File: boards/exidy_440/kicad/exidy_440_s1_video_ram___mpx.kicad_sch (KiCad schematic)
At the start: 11 parts

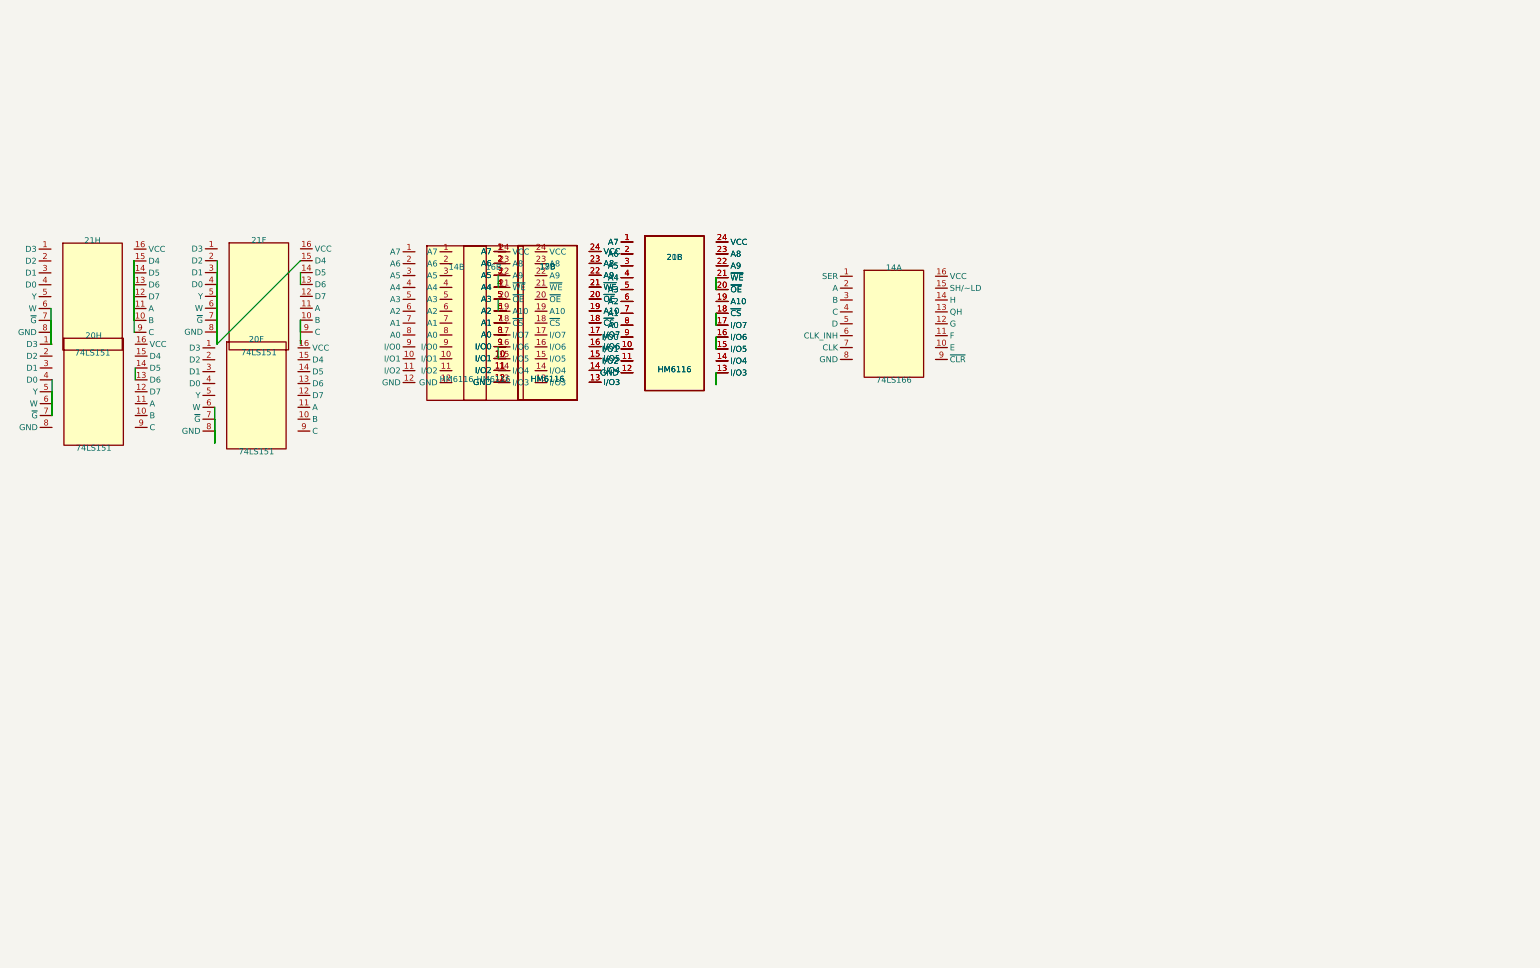
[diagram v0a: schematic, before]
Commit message: kicad export: emit Footprint property mapped from librarian package
Adds PACKAGE_TO_KICAD_FP table mapping librarian `package` strings
("DIP-14", "DIP-40", …) to KiCad stock footprint ids ("Package_DIP:
DIP-14_W7.62mm", "Package_DIP:DIP-40_W15.24mm", …). The table covers
every package currently in chips.json. Width convention: ≤20 pins →
0.3" (W7.62mm), ≥24 pins → 0.6" (W15.24mm), which matches the actual
chips in our librarian (≥24-pin parts are all memory/CPU, always 0.6"-
wide DIPs). Parts can override with an explicit `kicad_footprint`
field if a future chip breaks the rule.

Both lib_symbols and instance properties carry the footprint, so
`kicad-cli sch export bom` reports the correct land pattern per refdes.
No PCB-side library config needed — Package_DIP ships with KiCad.

Verified on dorado_base sheet 5 (still ERC PASS) and exidy_440 sheet 1
(blocking=0 unchanged); BOMs show every component mapped correctly.

Co-Authored-By: Claude Opus 4.7 (1M context) <noreply@anthropic.com>
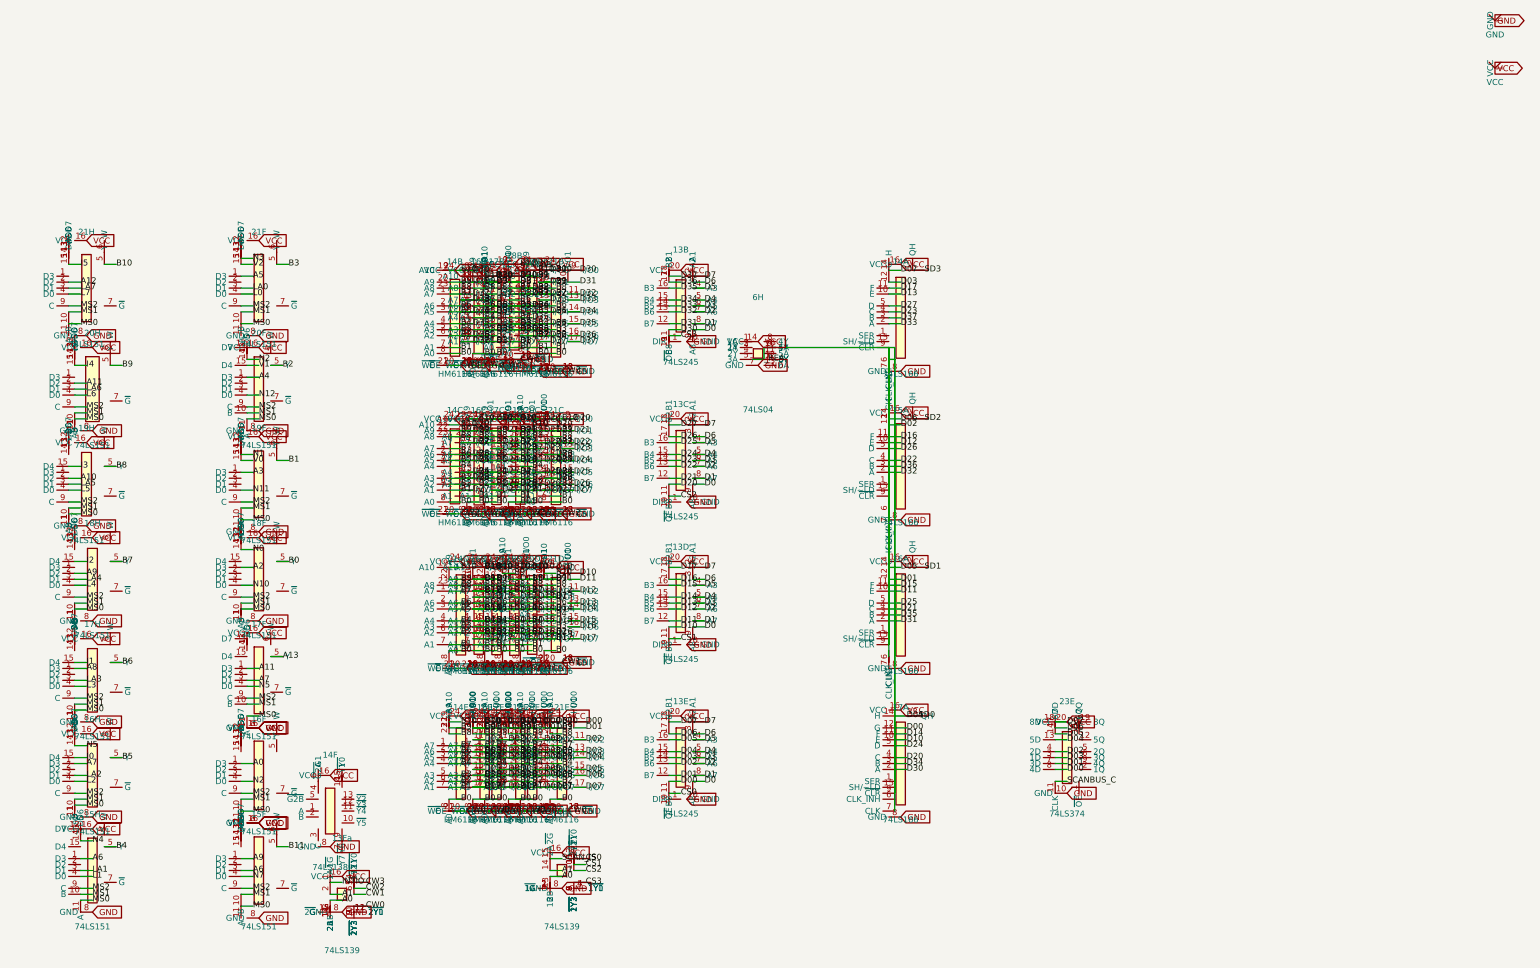
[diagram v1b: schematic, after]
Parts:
- added 13B: 74LS245, Package_DIP:DIP-20_W7.62mm, symbol user:_chip_13B
- added 13C: 74LS245, Package_DIP:DIP-20_W7.62mm, symbol user:_chip_13C
- added 13D: 74LS245, Package_DIP:DIP-20_W7.62mm, symbol user:_chip_13D
- added 13E: 74LS245, Package_DIP:DIP-20_W7.62mm, symbol user:_chip_13E
- added 13Fa: 74LS139, Package_DIP:DIP-16_W7.62mm, symbol user:_chip_13Fa
- added 13Fb: 74LS139, Package_DIP:DIP-16_W7.62mm, symbol user:_chip_13Fb
- added 14C: HM6116, Package_DIP:DIP-24_W15.24mm, symbol user:_chip_14C
- added 14D: HM6116, Package_DIP:DIP-24_W15.24mm, symbol user:_chip_14D
- added 14E: HM6116, Package_DIP:DIP-24_W15.24mm, symbol user:_chip_14E
- added 14F: 74LS138, Package_DIP:DIP-16_W7.62mm, symbol user:_chip_14F
- added 15A: 74LS166, Package_DIP:DIP-16_W7.62mm, symbol user:_chip_15A
- added 15F: 74LS151, Package_DIP:DIP-16_W7.62mm, symbol user:_chip_15F
- added 15H: 74LS151, Package_DIP:DIP-16_W7.62mm, symbol user:_chip_15H
- added 16A: 74LS166, Package_DIP:DIP-16_W7.62mm, symbol user:_chip_16A
- added 16C: HM6116, Package_DIP:DIP-24_W15.24mm, symbol user:_chip_16C
- added 16D: HM6116, Package_DIP:DIP-24_W15.24mm, symbol user:_chip_16D
- added 16E: HM6116, Package_DIP:DIP-24_W15.24mm, symbol user:_chip_16E
- added 16F: 74LS151, Package_DIP:DIP-16_W7.62mm, symbol user:_chip_16F
- added 16H: 74LS151, Package_DIP:DIP-16_W7.62mm, symbol user:_chip_16H
- added 17A: 74LS166, Package_DIP:DIP-16_W7.62mm, symbol user:_chip_17A
- added 17C: HM6116, Package_DIP:DIP-24_W15.24mm, symbol user:_chip_17C
- added 17D: HM6116, Package_DIP:DIP-24_W15.24mm, symbol user:_chip_17D
- added 17E: HM6116, Package_DIP:DIP-24_W15.24mm, symbol user:_chip_17E
- added 17F: 74LS151, Package_DIP:DIP-16_W7.62mm, symbol user:_chip_17F
- added 17H: 74LS151, Package_DIP:DIP-16_W7.62mm, symbol user:_chip_17H
- added 18C: HM6116, Package_DIP:DIP-24_W15.24mm, symbol user:_chip_18C
- added 18D: HM6116, Package_DIP:DIP-24_W15.24mm, symbol user:_chip_18D
- added 18E: HM6116, Package_DIP:DIP-24_W15.24mm, symbol user:_chip_18E
- added 18F: 74LS151, Package_DIP:DIP-16_W7.62mm, symbol user:_chip_18F
- added 18H: 74LS151, Package_DIP:DIP-16_W7.62mm, symbol user:_chip_18H
- added 19F: 74LS151, Package_DIP:DIP-16_W7.62mm, symbol user:_chip_19F
- added 19H: 74LS151, Package_DIP:DIP-16_W7.62mm, symbol user:_chip_19H
- added 20C: HM6116, Package_DIP:DIP-24_W15.24mm, symbol user:_chip_20C
- added 20D: HM6116, Package_DIP:DIP-24_W15.24mm, symbol user:_chip_20D
- added 20E: HM6116, Package_DIP:DIP-24_W15.24mm, symbol user:_chip_20E
- added 21C: HM6116, Package_DIP:DIP-24_W15.24mm, symbol user:_chip_21C
- added 21D: HM6116, Package_DIP:DIP-24_W15.24mm, symbol user:_chip_21D
- added 21E: HM6116, Package_DIP:DIP-24_W15.24mm, symbol user:_chip_21E
- added 23E: 74LS374, Package_DIP:DIP-20_W7.62mm, symbol user:_chip_23E
- added 6H: 74LS04, Package_DIP:DIP-14_W7.62mm, symbol user:_chip_6H
- 14A: footprint (none) -> Package_DIP:DIP-16_W7.62mm; symbol user:74LS166 -> user:_chip_14A
- 14B: footprint (none) -> Package_DIP:DIP-24_W15.24mm; symbol user:HM6116 -> user:_chip_14B
- 16B: footprint (none) -> Package_DIP:DIP-24_W15.24mm; symbol user:HM6116 -> user:_chip_16B
- 17B: footprint (none) -> Package_DIP:DIP-24_W15.24mm; symbol user:HM6116 -> user:_chip_17B
- 18B: footprint (none) -> Package_DIP:DIP-24_W15.24mm; symbol user:HM6116 -> user:_chip_18B
- 20B: footprint (none) -> Package_DIP:DIP-24_W15.24mm; symbol user:HM6116 -> user:_chip_20B
- 20F: footprint (none) -> Package_DIP:DIP-16_W7.62mm; symbol user:74LS151 -> user:_chip_20F
- 20H: footprint (none) -> Package_DIP:DIP-16_W7.62mm; symbol user:74LS151 -> user:_chip_20H
- 21B: footprint (none) -> Package_DIP:DIP-24_W15.24mm; symbol user:HM6116 -> user:_chip_21B
- 21F: footprint (none) -> Package_DIP:DIP-16_W7.62mm; symbol user:74LS151 -> user:_chip_21F
- 21H: footprint (none) -> Package_DIP:DIP-16_W7.62mm; symbol user:74LS151 -> user:_chip_21H
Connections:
- net GND: now reaches 17B.1 (A7), 18B.1 (A7)
- net GND: now also 14A.10 (E), 14A.11 (F), 14A.12 (G), 14A.14 (H), 14A.16 (VCC), 14A.2 (A), 14A.3 (B), 14A.4 (C), 14A.5 (D), 14A.8 (GND), 14B.1 (A7), 14B.10 (I/O1), 14B.11 (I/O2), 14B.12 (GND), 14B.13 (I/O3), 14B.14 (I/O4), 14B.15 (I/O5), 14B.16 (I/O6), 14B.17 (I/O7), 14B.18 (~{CS}), 14B.19 (A10), 14B.2 (A6), 14B.21 (~{WE}), 14B.22 (A9), 14B.23 (A8), 14B.24 (VCC), 14B.3 (A5), 14B.4 (A4), 14B.5 (A3), 14B.6 (A2), 14B.7 (A1), 14B.9 (I/O0), 16B.1 (A7), 16B.10 (I/O1), 16B.11 (I/O2), 16B.12 (GND), 16B.13 (I/O3), 16B.14 (I/O4), 16B.15 (I/O5), 16B.16 (I/O6), 16B.17 (I/O7), 16B.18 (~{CS}), 16B.19 (A10), 16B.2 (A6), 16B.21 (~{WE}), 16B.22 (A9), 16B.23 (A8), 16B.24 (VCC), 16B.3 (A5), 16B.4 (A4), 16B.5 (A3), 16B.6 (A2), 16B.7 (A1), 16B.9 (I/O0), 17B.10 (I/O1), 17B.11 (I/O2), 17B.12 (GND), 17B.13 (I/O3), 17B.14 (I/O4), 17B.15 (I/O5), 17B.16 (I/O6), 17B.17 (I/O7), 17B.18 (~{CS}), 17B.19 (A10), 17B.2 (A6), 17B.21 (~{WE}), 17B.22 (A9), 17B.23 (A8), 17B.24 (VCC), 17B.3 (A5), 17B.4 (A4), 17B.5 (A3), 17B.6 (A2), 17B.7 (A1), 17B.9 (I/O0), 18B.10 (I/O1), 18B.11 (I/O2), 18B.12 (GND), 18B.13 (I/O3), 18B.14 (I/O4), 18B.15 (I/O5), 18B.16 (I/O6), 18B.17 (I/O7), 18B.18 (~{CS}), 18B.19 (A10), 18B.2 (A6), 18B.21 (~{WE}), 18B.22 (A9), 18B.23 (A8), 18B.24 (VCC), 18B.3 (A5), 18B.4 (A4), 18B.5 (A3), 18B.6 (A2), 18B.7 (A1), 18B.9 (I/O0), 20B.1 (A7), 20B.10 (I/O1), 20B.11 (I/O2), 20B.12 (GND), 20B.13 (I/O3), 20B.14 (I/O4), 20B.15 (I/O5), 20B.16 (I/O6), 20B.17 (I/O7), 20B.18 (~{CS}), 20B.19 (A10), 20B.2 (A6), 20B.21 (~{WE}), 20B.22 (A9), 20B.23 (A8), 20B.24 (VCC), 20B.3 (A5), 20B.4 (A4), 20B.5 (A3), 20B.6 (A2), 20B.7 (A1), 20B.9 (I/O0), 20F.16 (VCC), 20F.5 (Y), 20F.8 (GND), 20H.16 (VCC), 20H.5 (Y), 20H.8 (GND), 21B.1 (A7), 21B.10 (I/O1), 21B.11 (I/O2), 21B.12 (GND), 21B.13 (I/O3), 21B.14 (I/O4), 21B.15 (I/O5), 21B.16 (I/O6), 21B.17 (I/O7), 21B.18 (~{CS}), 21B.19 (A10), 21B.2 (A6), 21B.21 (~{WE}), 21B.22 (A9), 21B.23 (A8), 21B.24 (VCC), 21B.3 (A5), 21B.4 (A4), 21B.5 (A3), 21B.6 (A2), 21B.7 (A1), 21B.9 (I/O0), 21F.16 (VCC), 21F.5 (Y), 21F.8 (GND), 21H.16 (VCC), 21H.5 (Y), 21H.8 (GND), 13B.10 (GND), 13B.11 (B8), 13B.12 (B7), 13B.13 (B6), 13B.14 (B5), 13B.15 (B4), 13B.16 (B3), 13B.17 (B2), 13B.18 (B1), 13B.20 (VCC), 13C.10 (GND), 13C.11 (B8), 13C.12 (B7), 13C.13 (B6), 13C.14 (B5), 13C.15 (B4), 13C.16 (B3), 13C.17 (B2), 13C.18 (B1), 13C.20 (VCC), 13D.10 (GND), 13D.11 (B8), 13D.12 (B7), 13D.13 (B6), 13D.14 (B5), 13D.15 (B4), 13D.16 (B3), 13D.17 (B2), 13D.18 (B1), 13D.20 (VCC), 13E.10 (GND), 13E.11 (B8), 13E.12 (B7), 13E.14 (B5), 13E.15 (B4), 13E.17 (B2), 13E.18 (B1), 13E.20 (VCC), 13Fa.10 (~{2Y2}), 13Fa.16 (VCC), 13Fa.4 (~{1Y0}), 13Fa.5 (~{1Y1}), 13Fa.6 (~{1Y2}), 13Fa.7 (~{1Y3}), 13Fa.8 (GND), 13Fa.9 (~{2Y3}), 13Fb.16 (VCC), 13Fb.8 (GND), 14C.1 (A7), 14C.10 (I/O1), 14C.11 (I/O2), 14C.12 (GND), 14C.13 (I/O3), 14C.14 (I/O4), 14C.15 (I/O5), 14C.16 (I/O6), 14C.17 (I/O7), 14C.18 (~{CS}), 14C.19 (A10), 14C.2 (A6), 14C.21 (~{WE}), 14C.22 (A9), 14C.23 (A8), 14C.24 (VCC), 14C.3 (A5), 14C.4 (A4), 14C.5 (A3), 14C.6 (A2), 14C.7 (A1), 14C.9 (I/O0), 14D.1 (A7), 14D.10 (I/O1), 14D.11 (I/O2), 14D.12 (GND), 14D.13 (I/O3), 14D.14 (I/O4), 14D.15 (I/O5), 14D.16 (I/O6), 14D.17 (I/O7), 14D.18 (~{CS}), 14D.19 (A10), 14D.2 (A6), 14D.21 (~{WE}), 14D.22 (A9), 14D.23 (A8), 14D.24 (VCC), 14D.3 (A5), 14D.4 (A4), 14D.5 (A3), 14D.6 (A2), 14D.7 (A1), 14D.9 (I/O0), 14E.1 (A7), 14E.10 (I/O1), 14E.12 (GND), 14E.13 (I/O3), 14E.14 (I/O4), 14E.16 (I/O6), 14E.17 (I/O7), 14E.18 (~{CS}), 14E.19 (A10), 14E.2 (A6), 14E.21 (~{WE}), 14E.22 (A9), 14E.23 (A8), 14E.24 (VCC), 14E.3 (A5), 14E.4 (A4), 14E.5 (A3), 14E.6 (A2), 14E.7 (A1), 14E.9 (I/O0), 14F.16 (VCC), 14F.8 (GND), 15A.10 (E), 15A.11 (F), 15A.14 (H), 15A.16 (VCC), 15A.2 (A), 15A.3 (B), 15A.4 (C), 15A.5 (D), 15A.8 (GND), 15F.16 (VCC), 15F.8 (GND), 15H.16 (VCC), 15H.5 (Y), 15H.8 (GND), 16A.10 (E), 16A.11 (F), 16A.12 (G), 16A.16 (VCC), 16A.2 (A), 16A.3 (B), 16A.4 (C), 16A.5 (D), 16A.8 (GND), 16C.1 (A7), 16C.10 (I/O1), 16C.11 (I/O2), 16C.12 (GND), 16C.13 (I/O3), 16C.14 (I/O4), 16C.15 (I/O5), 16C.16 (I/O6), 16C.17 (I/O7), 16C.18 (~{CS}), 16C.19 (A10), 16C.2 (A6), 16C.21 (~{WE}), 16C.22 (A9), 16C.23 (A8), 16C.24 (VCC), 16C.3 (A5), 16C.4 (A4), 16C.5 (A3), 16C.6 (A2), 16C.7 (A1), 16C.9 (I/O0), 16D.1 (A7), 16D.10 (I/O1), 16D.11 (I/O2), 16D.12 (GND), 16D.13 (I/O3), 16D.14 (I/O4), 16D.15 (I/O5), 16D.16 (I/O6), 16D.17 (I/O7), 16D.18 (~{CS}), 16D.19 (A10), 16D.2 (A6), 16D.21 (~{WE}), 16D.22 (A9), 16D.23 (A8), 16D.24 (VCC), 16D.3 (A5), 16D.4 (A4), 16D.5 (A3), 16D.6 (A2), 16D.7 (A1), 16D.9 (I/O0), 16E.1 (A7), 16E.10 (I/O1), 16E.12 (GND), 16E.13 (I/O3), 16E.14 (I/O4), 16E.16 (I/O6), 16E.17 (I/O7), 16E.18 (~{CS}), 16E.19 (A10), 16E.2 (A6), 16E.21 (~{WE}), 16E.22 (A9), 16E.23 (A8), 16E.24 (VCC), 16E.3 (A5), 16E.4 (A4), 16E.5 (A3), 16E.6 (A2), 16E.7 (A1), 16E.9 (I/O0), 16F.16 (VCC), 16F.8 (GND), 16H.16 (VCC), 16H.5 (Y), 16H.8 (GND), 17A.10 (E), 17A.11 (F), 17A.12 (G), 17A.13 (QH), 17A.14 (H), 17A.16 (VCC), 17A.2 (A), 17A.3 (B), 17A.4 (C), 17A.5 (D), 17A.8 (GND), 17C.1 (A7), 17C.10 (I/O1), 17C.11 (I/O2), 17C.12 (GND), 17C.13 (I/O3), 17C.14 (I/O4), 17C.15 (I/O5), 17C.16 (I/O6), 17C.17 (I/O7), 17C.18 (~{CS}), 17C.19 (A10), 17C.2 (A6), 17C.21 (~{WE}), 17C.22 (A9), 17C.23 (A8), 17C.24 (VCC), 17C.3 (A5), 17C.4 (A4), 17C.5 (A3), 17C.6 (A2), 17C.7 (A1), 17C.9 (I/O0), 17D.1 (A7), 17D.10 (I/O1), 17D.11 (I/O2), 17D.12 (GND), 17D.13 (I/O3), 17D.14 (I/O4), 17D.15 (I/O5), 17D.16 (I/O6), 17D.17 (I/O7)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
- net at 17B.20 (~{OE}): no longer 18B.20 (~{OE})
- net B0: now reaches 17B.8 (A0), 18B.8 (A0)
- net B0: now also 14B.8 (A0), 16B.8 (A0), 20B.8 (A0), 21B.8 (A0), 14C.8 (A0), 14D.8 (A0), 14E.8 (A0), 16C.8 (A0), 16D.8 (A0), 16E.8 (A0), 17C.8 (A0), 17D.8 (A0), 17E.8 (A0), 18C.8 (A0), 18D.8 (A0), 18E.8 (A0), 18F.5 (Y), 20C.8 (A0), 20D.8 (A0), 20E.8 (A0), 21C.8 (A0), 21D.8 (A0), 21E.8 (A0)
- net A12: now reaches 21H.2 (D2)
- net LA7: now reaches 21H.3 (D1)
- net L7: now reaches 21H.4 (D0)
- net at 14B.20 (~{OE}): no longer 14B.19 (A10)
- net A5: now reaches 21F.1 (D3)
- net MS1: now reaches 21F.10 (B)
- net MS1: now also 20F.10 (B), 20H.10 (B), 21H.10 (B), 15F.10 (B), 15H.10 (B), 16F.10 (B), 16H.10 (B), 17F.10 (B), 17H.10 (B), 18F.10 (B), 18H.10 (B), 19F.10 (B), 19H.10 (B); no longer 21F.9 (C)
- net MS0: now reaches 21F.11 (A)
- net MS0: now also 20F.11 (A), 20H.11 (A), 21H.11 (A), 15F.11 (A), 15H.11 (A), 16F.11 (A), 16H.11 (A), 17F.11 (A), 17H.11 (A), 18F.11 (A), 18H.11 (A), 19F.11 (A), 19H.11 (A)
- net at 21F.13 (D6): no longer 21F.14 (D5)
- net A4: now reaches 20F.1 (D3)
- net N2: now reaches 20F.14 (D5)
- net N2: now also 16F.4 (D0)
- net V1: now reaches 20F.15 (D4)
- net N12: now reaches 20F.4 (D0)
- net MS2: now reaches 20F.9 (C)
- net MS2: now also 20H.9 (C), 21F.9 (C), 21H.9 (C), 15F.9 (C), 15H.9 (C), 16F.9 (C), 16H.9 (C), 17F.9 (C), 17H.9 (C), 18F.9 (C), 18H.9 (C), 19F.9 (C), 19H.9 (C)
- net SD3: now reaches 14A.13 (QH)
- net _REA: now reaches 14A.7 (CLK)
- net _REA: now also 14A.9 (~{CLR}), 15A.7 (CLK), 15A.9 (~{CLR}), 16A.7 (CLK), 16A.9 (~{CLR}), 17A.7 (CLK), 17A.9 (~{CLR}), 6H.10 (5Y), 6H.12 (6Y), 6H.5 (3A), 6H.6 (3Y), 6H.9 (4A)
- net at 20H.13 (D6): no longer 20H.14 (D5)
- net I4: now reaches 20H.15 (D4)
- net A11: now reaches 20H.2 (D2)
- net A11: now also 17F.1 (D3)
- net LA6: now reaches 20H.3 (D1)
- net L6: now reaches 20H.4 (D0)
- new net: 6H.2 (1Y), 6H.3 (2A)
- new net: 13Fa.11 (~{2Y1}), 13Fa.12 (~{2Y0})
- new net: 13Fa.13 (2B), 13Fa.14 (2A)
- new net: 13Fb.1 (~{1G}), 13Fb.2 (1A)
- new net: 13Fb.4 (~{1Y0}), 13Fb.5 (~{1Y1})
- new net A0: 13Fa.3 (1B), 13Fb.13 (2B), 16F.1 (D3)
- new net A1: 13Fa.2 (1A), 13Fb.14 (2A)
- new net A10: 19H.2 (D2)
- new net A13: 17F.5 (Y)
- new net A2: 18F.1 (D3)
- new net A3: 19F.1 (D3)
- new net A6: 15F.3 (D1), 15H.1 (D3)
- new net A7: 16H.1 (D3), 17F.3 (D1)
- new net A8: 17H.1 (D3)
- new net A9: 15F.1 (D3), 18H.2 (D2)
- new net B11: 15F.5 (Y)
- new net CS0: 13E.19 (~{OE}), 13Fb.12 (~{2Y0})
- new net CS1: 13D.19 (~{OE}), 13Fb.11 (~{2Y1})
- new net CS2: 13C.19 (~{OE}), 13Fb.10 (~{2Y2})
- new net CS3: 13B.19 (~{OE}), 13Fb.6 (~{1Y2}), 13Fb.7 (~{1Y3}), 13Fb.9 (~{2Y3})
- new net D0: 13B.9 (A8), 13C.9 (A8), 13D.9 (A8), 13E.9 (A8)
- new net D02: 13E.13 (B6), 14E.11 (I/O2), 15A.12 (G), 16E.11 (I/O2), 17E.11 (I/O2), 18E.11 (I/O2), 20E.11 (I/O2), 21E.11 (I/O2), 23E.4 (2D)
- new net D05: 13E.16 (B3), 14E.15 (I/O5), 16A.14 (H), 16E.15 (I/O5), 17E.15 (I/O5), 18E.15 (I/O5), 20E.15 (I/O5), 21E.15 (I/O5), 23E.14 (6D)
- new net D1: 13B.8 (A7), 13C.8 (A7), 13D.8 (A7), 13E.8 (A7)
- new net D2: 13B.7 (A6), 13C.7 (A6), 13D.7 (A6), 13E.7 (A6)
- new net D3: 13B.6 (A5), 13C.6 (A5), 13D.6 (A5), 13E.6 (A5)
- new net D4: 13B.5 (A4), 13C.5 (A4), 13D.5 (A4), 13E.5 (A4)
- new net D5: 13B.4 (A3), 13C.4 (A3), 13D.4 (A3), 13E.4 (A3)
- new net D6: 13B.3 (A2), 13C.3 (A2), 13D.3 (A2), 13E.3 (A2)
- new net D7: 13B.2 (A1), 13C.2 (A1), 13D.2 (A1), 13E.2 (A1)
- new net I0: 16H.15 (D4)
- new net I1: 17H.15 (D4)
- new net I2: 18H.15 (D4)
- new net I3: 19H.15 (D4)
- new net I5: 21H.15 (D4)
- new net INTIO: 13Fa.1 (~{1G})
- new net L0: 21F.4 (D0)
- new net L1: 15H.4 (D0)
- new net L2: 16H.4 (D0)
- new net L3: 17H.4 (D0)
- new net L4: 18H.4 (D0)
- new net L5: 19H.4 (D0)
- new net LA0: 21F.3 (D1)
- new net LA1: 15H.3 (D1)
- new net LA2: 16H.3 (D1)
- new net LA3: 17H.3 (D1)
- new net LA4: 18H.3 (D1)
- new net LA5: 19H.3 (D1)
- new net N0: 18F.14 (D5)
- new net N1: 19F.14 (D5)
- new net N10: 18F.4 (D0)
- new net N11: 19F.4 (D0)
- new net N3: 21F.14 (D5)
- new net N4: 15H.14 (D5)
- new net N5: 16H.14 (D5), 17F.4 (D0)
- new net N7: 15F.4 (D0)
- new net SCANBUS_C: 23E.11 (CLK)
- new net SCAN_IS: 13Fb.15 (~{2G})
- new net SD1: 16A.13 (QH)
- new net SD2: 15A.13 (QH)
- new net V0: 19F.15 (D4)
- new net V2: 21F.15 (D4)
- now unconnected: 20B.20 (~{OE}), 20F.6 (W), 20F.7 (~{G}), 21B.20 (~{OE}), 21F.2 (D2), 21F.6 (W), 21F.7 (~{G}), 21H.12 (D7), 21H.13 (D6), 21H.14 (D5)
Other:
- moved on the sheet: 14A, 20F, 20H, 21F, 21H

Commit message: kicad export: fix pin-tip / polyline snap mismatch (1.27 mm off-grid)
Two code paths emitted absolute mm coords differently:

  pin tip   = _snap(M + cx_px*s) + _snap((ix-cx_px)*s)      # double-snap
  polyline  = _snap(M + p[0]*s)                              # single-snap

`_snap(a) + _snap(b) != _snap(a+b)` in general — the difference is 0 or
±1 grid unit. On Z80 SBC, a hand-traced wire from J1.2 to U1.14 had its
endpoint at the polyline's snapped coord (71.12, 76.20) while the pin
tip lived at the double-snapped coord (72.39, 74.93). KiCad reported
wire_dangling and 8 other short wires had the same workaround applied
(converted to label nets to dodge it).

Fix:
- synth_faithful_symbol now derives lib-symbol pin coords from the
  absolute pin tip (single-snap) minus the instance origin, instead of
  snapping the local offset directly. The local pin offset is no longer
  guaranteed to be a whole grid unit — body and pin can drift up to
  ~0.6 mm relative to each other — but the absolute pin tip is now
  always on grid AND agrees with every other coord-emitting path.
- gen_sch's faithful branch uses the same single-snap formula for
  pin_endpoint_mm.

This makes pin tips, polyline points, junctions, and discrete pins all
share one snap convention. Validated on Z80 SBC: RS232_TX (a workaround
label) converted back to wire + path produces wire_dangling=0.

Regression: dorado_base sheets 5/7/8, z80_sbc sheet 1, exidy_440 sheet 1
all stay blocking=0. Pre-existing graph wiring errors (pin_to_pin,
multiple_net_names) unchanged.

Removes bugs/polyline-pin-snap-mismatch.md.

Co-Authored-By: Claude Opus 4.7 (1M context) <noreply@anthropic.com>
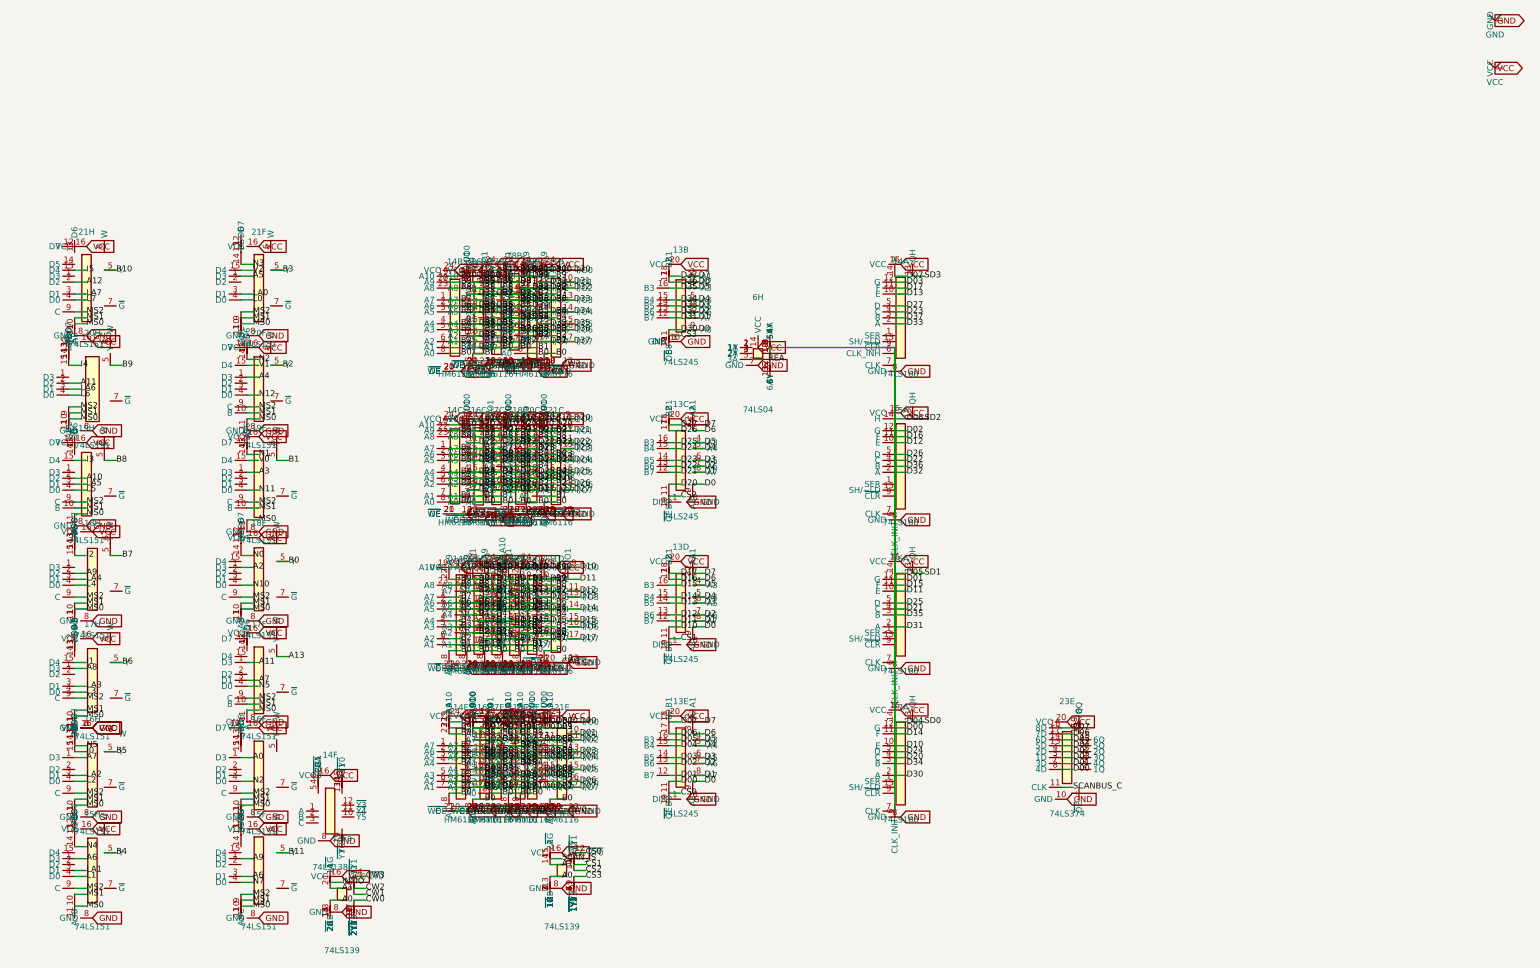
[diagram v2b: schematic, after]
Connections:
- net CS3: no longer 13Fb.6 (~{1Y2}), 13Fb.7 (~{1Y3})
- net GND: now also 13B.1 (DIR), 14B.20 (~{OE}), 14C.20 (~{OE}), 16B.20 (~{OE}), 17E.20 (~{OE}), 20B.20 (~{OE}); no longer 13B.12 (B7), 13B.13 (B6), 13B.14 (B5), 13B.15 (B4), 13B.16 (B3), 13B.17 (B2), 13B.18 (B1), 13C.12 (B7), 13C.13 (B6), 13C.14 (B5), 13C.15 (B4), 13C.16 (B3), 13C.17 (B2), 13C.18 (B1), 13D.12 (B7), 13D.13 (B6), 13D.14 (B5), 13D.15 (B4), 13D.16 (B3), 13D.17 (B2), 13D.18 (B1), 13E.12 (B7), 13E.14 (B5), 13E.15 (B4), 13E.17 (B2), 13E.18 (B1), 13Fa.10 (~{2Y2}), 13Fa.9 (~{2Y3}), 14A.10 (E), 14A.11 (F), 14A.12 (G), 14A.14 (H), 14A.2 (A), 14A.3 (B), 14A.4 (C), 14A.5 (D), 14B.1 (A7), 14B.10 (I/O1), 14B.11 (I/O2), 14B.13 (I/O3), 14B.14 (I/O4), 14B.15 (I/O5), 14B.16 (I/O6), 14B.17 (I/O7), 14B.2 (A6), 14B.22 (A9), 14B.23 (A8), 14B.3 (A5), 14B.4 (A4), 14B.5 (A3), 14B.6 (A2), 14B.7 (A1), 14C.1 (A7), 14C.10 (I/O1), 14C.11 (I/O2), 14C.13 (I/O3), 14C.14 (I/O4), 14C.15 (I/O5), 14C.16 (I/O6), 14C.17 (I/O7), 14C.18 (~{CS}), 14C.2 (A6), 14C.22 (A9), 14C.23 (A8), 14C.3 (A5), 14C.4 (A4), 14C.5 (A3), 14C.6 (A2), 14C.7 (A1), 14D.1 (A7), 14D.10 (I/O1), 14D.11 (I/O2), 14D.13 (I/O3), 14D.14 (I/O4), 14D.15 (I/O5), 14D.16 (I/O6), 14D.17 (I/O7), 14D.2 (A6), 14D.22 (A9), 14D.23 (A8), 14D.3 (A5), 14D.4 (A4), 14D.5 (A3), 14D.6 (A2), 14D.7 (A1), 14E.1 (A7), 14E.10 (I/O1), 14E.13 (I/O3), 14E.14 (I/O4), 14E.16 (I/O6), 14E.17 (I/O7), 14E.2 (A6), 14E.22 (A9), 14E.23 (A8), 14E.3 (A5), 14E.4 (A4), 14E.5 (A3), 14E.6 (A2), 14E.7 (A1), 15A.10 (E), 15A.11 (F), 15A.14 (H), 15A.2 (A), 15A.3 (B), 15A.4 (C), 15A.5 (D), 15H.5 (Y), 16A.10 (E), 16A.11 (F), 16A.12 (G), 16A.2 (A), 16A.3 (B), 16A.4 (C), 16A.5 (D), 16B.1 (A7), 16B.10 (I/O1), 16B.11 (I/O2), 16B.13 (I/O3), 16B.14 (I/O4), 16B.15 (I/O5), 16B.16 (I/O6), 16B.17 (I/O7), 16B.2 (A6), 16B.22 (A9), 16B.23 (A8), 16B.3 (A5), 16B.4 (A4), 16B.5 (A3), 16B.6 (A2), 16B.7 (A1), 16C.1 (A7), 16C.10 (I/O1), 16C.11 (I/O2), 16C.13 (I/O3), 16C.14 (I/O4), 16C.15 (I/O5), 16C.16 (I/O6), 16C.17 (I/O7), 16C.2 (A6), 16C.22 (A9), 16C.23 (A8), 16C.3 (A5), 16C.4 (A4), 16C.5 (A3), 16C.6 (A2), 16C.7 (A1), 16D.1 (A7), 16D.10 (I/O1), 16D.11 (I/O2), 16D.13 (I/O3), 16D.14 (I/O4), 16D.15 (I/O5), 16D.16 (I/O6), 16D.17 (I/O7), 16D.2 (A6), 16D.22 (A9), 16D.23 (A8), 16D.3 (A5), 16D.4 (A4), 16D.5 (A3), 16D.6 (A2), 16D.7 (A1), 16E.1 (A7), 16E.10 (I/O1), 16E.13 (I/O3), 16E.14 (I/O4), 16E.16 (I/O6), 16E.17 (I/O7), 16E.18 (~{CS}), 16E.2 (A6), 16E.22 (A9), 16E.23 (A8), 16E.3 (A5), 16E.4 (A4), 16E.5 (A3), 16E.6 (A2), 16E.7 (A1), 16H.5 (Y), 17A.11 (F), 17A.13 (QH), 17A.14 (H), 17A.3 (B), 17A.5 (D), 17B.1 (A7), 17B.10 (I/O1), 17B.11 (I/O2), 17B.13 (I/O3), 17B.14 (I/O4), 17B.15 (I/O5), 17B.16 (I/O6), 17B.17 (I/O7), 17B.2 (A6), 17B.22 (A9), 17B.23 (A8), 17B.3 (A5), 17B.4 (A4), 17B.5 (A3), 17B.6 (A2), 17B.7 (A1), 17C.1 (A7), 17C.10 (I/O1), 17C.11 (I/O2), 17C.13 (I/O3), 17C.14 (I/O4), 17C.15 (I/O5), 17C.16 (I/O6), 17C.17 (I/O7), 17C.2 (A6), 17C.22 (A9), 17C.23 (A8), 17C.3 (A5), 17C.4 (A4), 17C.5 (A3), 17C.6 (A2), 17C.7 (A1), 17D.1 (A7), 17D.10 (I/O1), 17D.11 (I/O2), 17D.13 (I/O3), 17D.14 (I/O4), 17D.15 (I/O5), 17D.16 (I/O6), 17D.17 (I/O7), 17D.2 (A6), 17D.22 (A9), 17D.23 (A8), 17D.3 (A5), 17D.4 (A4), 17D.5 (A3), 17D.6 (A2), 17D.7 (A1), 17E.1 (A7), 17E.10 (I/O1), 17E.13 (I/O3), 17E.14 (I/O4), 17E.16 (I/O6), 17E.17 (I/O7), 17E.18 (~{CS}), 17E.2 (A6), 17E.22 (A9), 17E.23 (A8), 17E.3 (A5), 17E.4 (A4), 17E.5 (A3), 17E.6 (A2), 17E.7 (A1), 17H.5 (Y), 18B.1 (A7), 18B.10 (I/O1), 18B.11 (I/O2), 18B.13 (I/O3), 18B.14 (I/O4), 18B.15 (I/O5), 18B.16 (I/O6), 18B.17 (I/O7), 18B.2 (A6), 18B.22 (A9), 18B.23 (A8), 18B.3 (A5), 18B.4 (A4), 18B.5 (A3), 18B.6 (A2), 18B.7 (A1), 18C.1 (A7), 18C.10 (I/O1), 18C.11 (I/O2), 18C.13 (I/O3), 18C.14 (I/O4), 18C.15 (I/O5), 18C.16 (I/O6), 18C.17 (I/O7), 18C.18 (~{CS}), 18C.2 (A6), 18C.22 (A9), 18C.23 (A8), 18C.3 (A5), 18C.4 (A4), 18C.5 (A3), 18C.6 (A2), 18C.7 (A1), 18D.1 (A7), 18D.10 (I/O1), 18D.11 (I/O2), 18D.13 (I/O3), 18D.14 (I/O4), 18D.15 (I/O5), 18D.16 (I/O6), 18D.17 (I/O7), 18D.2 (A6), 18D.22 (A9), 18D.23 (A8), 18D.3 (A5), 18D.4 (A4), 18D.5 (A3), 18D.6 (A2), 18D.7 (A1), 18E.1 (A7), 18E.10 (I/O1), 18E.13 (I/O3), 18E.14 (I/O4), 18E.16 (I/O6), 18E.17 (I/O7), 18E.2 (A6), 18E.22 (A9), 18E.23 (A8), 18E.3 (A5), 18E.4 (A4), 18E.5 (A3), 18E.6 (A2), 18E.7 (A1), 18H.5 (Y), 19F.5 (Y), 19H.5 (Y), 20B.1 (A7), 20B.10 (I/O1), 20B.11 (I/O2), 20B.13 (I/O3), 20B.14 (I/O4), 20B.15 (I/O5), 20B.16 (I/O6), 20B.17 (I/O7), 20B.2 (A6), 20B.22 (A9), 20B.23 (A8), 20B.3 (A5), 20B.4 (A4), 20B.5 (A3), 20B.6 (A2), 20B.7 (A1), 20C.1 (A7), 20C.10 (I/O1), 20C.11 (I/O2), 20C.13 (I/O3), 20C.14 (I/O4), 20C.15 (I/O5), 20C.16 (I/O6), 20C.17 (I/O7), 20C.2 (A6), 20C.22 (A9), 20C.23 (A8), 20C.3 (A5), 20C.4 (A4), 20C.5 (A3), 20C.6 (A2), 20C.7 (A1), 20D.1 (A7), 20D.10 (I/O1), 20D.11 (I/O2), 20D.13 (I/O3), 20D.14 (I/O4), 20D.15 (I/O5), 20D.16 (I/O6), 20D.17 (I/O7), 20D.2 (A6), 20D.22 (A9), 20D.23 (A8), 20D.3 (A5), 20D.4 (A4), 20D.5 (A3), 20D.6 (A2), 20D.7 (A1), 20E.1 (A7), 20E.10 (I/O1), 20E.13 (I/O3), 20E.14 (I/O4), 20E.16 (I/O6), 20E.17 (I/O7), 20E.2 (A6), 20E.22 (A9), 20E.23 (A8), 20E.3 (A5), 20E.4 (A4), 20E.5 (A3), 20E.6 (A2), 20E.7 (A1), 20F.5 (Y), 20H.5 (Y), 21B.1 (A7), 21B.10 (I/O1), 21B.11 (I/O2), 21B.13 (I/O3), 21B.14 (I/O4), 21B.15 (I/O5), 21B.16 (I/O6), 21B.17 (I/O7), 21B.18 (~{CS}), 21B.2 (A6), 21B.22 (A9), 21B.23 (A8), 21B.3 (A5), 21B.4 (A4), 21B.5 (A3), 21B.6 (A2), 21B.7 (A1), 21C.1 (A7), 21C.10 (I/O1), 21C.11 (I/O2), 21C.13 (I/O3), 21C.14 (I/O4), 21C.15 (I/O5)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
- net _REA: no longer 14A.7 (CLK), 14A.9 (~{CLR}), 15A.7 (CLK), 15A.9 (~{CLR}), 16A.7 (CLK), 16A.9 (~{CLR}), 17A.7 (CLK), 17A.9 (~{CLR}), 6H.10 (5Y), 6H.12 (6Y), 6H.6 (3Y), 6H.9 (4A)
- net at 21B.20 (~{OE}): now also 21B.18 (~{CS})
- net at 6H.1 (1A): now also 6H.2 (1Y)
- net at 6H.11 (5A): now also 6H.10 (5Y)
- net at 6H.3 (2A): now also 6H.4 (2Y); no longer 6H.2 (1Y)
- net at 6H.8 (4Y): now also 14A.7 (CLK), 14A.9 (~{CLR}), 15A.7 (CLK), 15A.9 (~{CLR}), 16A.7 (CLK), 16A.9 (~{CLR}), 17A.7 (CLK), 17A.9 (~{CLR}), 6H.12 (6Y), 6H.6 (3Y), 6H.9 (4A)
- net at 18C.20 (~{OE}): now also 18C.18 (~{CS})
- net at 21E.20 (~{OE}): now also 21E.18 (~{CS})
- net at 21C.20 (~{OE}): now also 21C.18 (~{CS})
- net at 13Fa.11 (~{2Y1}), 13Fa.12 (~{2Y0}): now also 13Fa.10 (~{2Y2}), 13Fa.9 (~{2Y3})
- net at 13Fa.13 (2B), 13Fa.14 (2A): now also 13Fa.15 (~{2G})
- net at 13Fb.1 (~{1G}), 13Fb.2 (1A): now also 13Fb.3 (1B)
- net at 13Fb.4 (~{1Y0}), 13Fb.5 (~{1Y1}): now also 13Fb.6 (~{1Y2}), 13Fb.7 (~{1Y3})
- net at 16E.20 (~{OE}): now also 16E.18 (~{CS})
- net D02 renamed B6
- net B6: now also 13B.12 (B7), 13B.13 (B6), 13B.14 (B5), 13C.12 (B7), 13C.13 (B6), 13C.14 (B5), 13D.12 (B7), 13D.13 (B6), 13D.14 (B5), 13E.12 (B7), 13E.14 (B5), 14A.10 (E), 14A.12 (G), 14A.2 (A), 14A.4 (C), 14B.1 (A7), 14B.10 (I/O1), 14B.11 (I/O2), 14B.13 (I/O3), 14B.2 (A6), 14B.22 (A9), 14B.23 (A8), 14C.1 (A7), 14C.10 (I/O1), 14C.11 (I/O2), 14C.13 (I/O3), 14C.2 (A6), 14C.22 (A9), 14C.23 (A8), 14D.1 (A7), 14D.10 (I/O1), 14D.11 (I/O2), 14D.13 (I/O3), 14D.2 (A6), 14D.22 (A9), 14D.23 (A8), 14E.1 (A7), 14E.10 (I/O1), 14E.13 (I/O3), 14E.2 (A6), 14E.22 (A9), 14E.23 (A8), 15A.10 (E), 15A.2 (A), 15A.4 (C), 16A.10 (E), 16A.12 (G), 16A.2 (A), 16A.4 (C), 16B.1 (A7), 16B.10 (I/O1), 16B.11 (I/O2), 16B.13 (I/O3), 16B.2 (A6), 16B.22 (A9), 16B.23 (A8), 16C.1 (A7), 16C.10 (I/O1), 16C.11 (I/O2), 16C.13 (I/O3), 16C.2 (A6), 16C.22 (A9), 16C.23 (A8), 16D.1 (A7), 16D.10 (I/O1), 16D.11 (I/O2), 16D.13 (I/O3), 16D.2 (A6), 16D.22 (A9), 16D.23 (A8), 16E.1 (A7), 16E.10 (I/O1), 16E.13 (I/O3), 16E.2 (A6), 16E.22 (A9), 16E.23 (A8), 17B.1 (A7), 17B.10 (I/O1), 17B.11 (I/O2), 17B.13 (I/O3), 17B.2 (A6), 17B.22 (A9), 17B.23 (A8), 17C.1 (A7), 17C.10 (I/O1), 17C.11 (I/O2), 17C.13 (I/O3), 17C.2 (A6), 17C.22 (A9), 17C.23 (A8), 17D.1 (A7), 17D.10 (I/O1), 17D.11 (I/O2), 17D.13 (I/O3), 17D.2 (A6), 17D.22 (A9), 17D.23 (A8), 17E.1 (A7), 17E.10 (I/O1), 17E.13 (I/O3), 17E.2 (A6), 17E.22 (A9), 17E.23 (A8), 17H.5 (Y), 18B.1 (A7), 18B.10 (I/O1), 18B.11 (I/O2), 18B.13 (I/O3), 18B.2 (A6), 18B.22 (A9), 18B.23 (A8), 18C.1 (A7), 18C.10 (I/O1), 18C.11 (I/O2), 18C.13 (I/O3), 18C.2 (A6), 18C.22 (A9), 18C.23 (A8), 18D.1 (A7), 18D.10 (I/O1), 18D.11 (I/O2), 18D.13 (I/O3), 18D.2 (A6), 18D.22 (A9), 18D.23 (A8), 18E.1 (A7), 18E.10 (I/O1), 18E.13 (I/O3), 18E.2 (A6), 18E.22 (A9), 18E.23 (A8), 18H.5 (Y), 19H.5 (Y), 20B.1 (A7), 20B.10 (I/O1), 20B.11 (I/O2), 20B.13 (I/O3), 20B.2 (A6), 20B.22 (A9), 20B.23 (A8), 20C.1 (A7), 20C.10 (I/O1), 20C.11 (I/O2), 20C.13 (I/O3), 20C.2 (A6), 20C.22 (A9), 20C.23 (A8), 20D.1 (A7), 20D.10 (I/O1), 20D.11 (I/O2), 20D.13 (I/O3), 20D.2 (A6), 20D.22 (A9), 20D.23 (A8), 20E.1 (A7), 20E.10 (I/O1), 20E.13 (I/O3), 20E.2 (A6), 20E.22 (A9), 20E.23 (A8), 20H.5 (Y), 21B.1 (A7), 21B.10 (I/O1), 21B.11 (I/O2), 21B.13 (I/O3), 21B.2 (A6), 21B.22 (A9), 21B.23 (A8), 21C.1 (A7), 21C.10 (I/O1), 21C.11 (I/O2), 21C.13 (I/O3), 21C.2 (A6), 21C.22 (A9), 21C.23 (A8), 21D.1 (A7), 21D.10 (I/O1), 21D.11 (I/O2), 21D.13 (I/O3), 21D.2 (A6), 21D.22 (A9), 21D.23 (A8), 21E.1 (A7), 21E.10 (I/O1), 21E.13 (I/O3), 21E.2 (A6), 21E.22 (A9), 21E.23 (A8), 23E.3 (1D), 23E.7 (3D)
- net D05 renamed B1
- net B1: now also 13B.16 (B3), 13B.17 (B2), 13B.18 (B1), 13C.16 (B3), 13C.17 (B2), 13C.18 (B1), 13D.16 (B3), 13D.17 (B2), 13D.18 (B1), 13E.17 (B2), 13E.18 (B1), 14A.11 (F), 14A.14 (H), 14A.3 (B), 14A.5 (D), 14B.15 (I/O5), 14B.16 (I/O6), 14B.17 (I/O7), 14B.4 (A4), 14B.5 (A3), 14B.6 (A2), 14B.7 (A1), 14C.15 (I/O5), 14C.16 (I/O6), 14C.17 (I/O7), 14C.4 (A4), 14C.5 (A3), 14C.6 (A2), 14C.7 (A1), 14D.15 (I/O5), 14D.16 (I/O6), 14D.17 (I/O7), 14D.4 (A4), 14D.5 (A3), 14D.6 (A2), 14D.7 (A1), 14E.16 (I/O6), 14E.17 (I/O7), 14E.4 (A4), 14E.5 (A3), 14E.6 (A2), 14E.7 (A1), 15A.11 (F), 15A.14 (H), 15A.3 (B), 15A.5 (D), 15H.5 (Y), 16A.11 (F), 16A.3 (B), 16A.5 (D), 16B.15 (I/O5), 16B.16 (I/O6), 16B.17 (I/O7), 16B.4 (A4), 16B.5 (A3), 16B.6 (A2), 16B.7 (A1), 16C.15 (I/O5), 16C.16 (I/O6), 16C.17 (I/O7), 16C.4 (A4), 16C.5 (A3), 16C.6 (A2), 16C.7 (A1), 16D.15 (I/O5), 16D.16 (I/O6), 16D.17 (I/O7), 16D.4 (A4), 16D.5 (A3), 16D.6 (A2), 16D.7 (A1), 16E.16 (I/O6), 16E.17 (I/O7), 16E.4 (A4), 16E.5 (A3), 16E.6 (A2), 16E.7 (A1), 17B.15 (I/O5), 17B.16 (I/O6), 17B.17 (I/O7), 17B.4 (A4), 17B.5 (A3), 17B.6 (A2), 17B.7 (A1), 17C.15 (I/O5), 17C.16 (I/O6), 17C.17 (I/O7), 17C.4 (A4), 17C.5 (A3), 17C.6 (A2), 17C.7 (A1), 17D.15 (I/O5), 17D.16 (I/O6), 17D.17 (I/O7), 17D.4 (A4), 17D.5 (A3), 17D.6 (A2), 17D.7 (A1), 17E.16 (I/O6), 17E.17 (I/O7), 17E.4 (A4), 17E.5 (A3), 17E.6 (A2), 17E.7 (A1), 18B.15 (I/O5), 18B.16 (I/O6), 18B.17 (I/O7), 18B.4 (A4), 18B.5 (A3), 18B.6 (A2), 18B.7 (A1), 18C.15 (I/O5), 18C.16 (I/O6), 18C.17 (I/O7), 18C.4 (A4), 18C.5 (A3), 18C.6 (A2), 18C.7 (A1), 18D.15 (I/O5), 18D.16 (I/O6), 18D.17 (I/O7), 18D.4 (A4), 18D.5 (A3), 18D.6 (A2), 18D.7 (A1), 18E.16 (I/O6), 18E.17 (I/O7), 18E.4 (A4), 18E.5 (A3), 18E.6 (A2), 18E.7 (A1), 19F.5 (Y), 20B.15 (I/O5), 20B.16 (I/O6), 20B.17 (I/O7), 20B.4 (A4), 20B.5 (A3), 20B.6 (A2), 20B.7 (A1), 20C.15 (I/O5), 20C.16 (I/O6), 20C.17 (I/O7), 20C.4 (A4), 20C.5 (A3), 20C.6 (A2), 20C.7 (A1), 20D.15 (I/O5), 20D.16 (I/O6), 20D.17 (I/O7), 20D.4 (A4), 20D.5 (A3), 20D.6 (A2), 20D.7 (A1), 20E.16 (I/O6), 20E.17 (I/O7), 20E.4 (A4), 20E.5 (A3), 20E.6 (A2), 20E.7 (A1), 20F.5 (Y), 21B.15 (I/O5), 21B.16 (I/O6), 21B.17 (I/O7), 21B.4 (A4), 21B.5 (A3), 21B.6 (A2), 21B.7 (A1), 21C.15 (I/O5), 21C.16 (I/O6), 21C.17 (I/O7), 21C.4 (A4), 21C.5 (A3), 21C.6 (A2), 21C.7 (A1), 21D.15 (I/O5), 21D.16 (I/O6), 21D.17 (I/O7), 21D.4 (A4), 21D.5 (A3), 21D.6 (A2), 21D.7 (A1), 21E.16 (I/O6), 21E.17 (I/O7), 21E.4 (A4), 21E.5 (A3), 21E.6 (A2), 21E.7 (A1), 21F.5 (Y), 23E.17 (7D), 23E.18 (8D)
- new net B5: 13B.15 (B4), 13C.15 (B4), 13D.15 (B4), 13E.15 (B4), 14B.14 (I/O4), 14B.3 (A5), 14C.14 (I/O4), 14C.3 (A5), 14D.14 (I/O4), 14D.3 (A5), 14E.14 (I/O4), 14E.3 (A5), 16B.14 (I/O4), 16B.3 (A5), 16C.14 (I/O4), 16C.3 (A5), 16D.14 (I/O4), 16D.3 (A5), 16E.14 (I/O4), 16E.3 (A5), 16H.5 (Y), 17A.11 (F), 17A.14 (H), 17A.3 (B), 17A.5 (D), 17B.14 (I/O4), 17B.3 (A5), 17C.14 (I/O4), 17C.3 (A5), 17D.14 (I/O4), 17D.3 (A5), 17E.14 (I/O4), 17E.3 (A5), 18B.14 (I/O4), 18B.3 (A5), 18C.14 (I/O4), 18C.3 (A5), 18D.14 (I/O4), 18D.3 (A5), 18E.14 (I/O4), 18E.3 (A5), 20B.14 (I/O4), 20B.3 (A5), 20C.14 (I/O4), 20C.3 (A5), 20D.14 (I/O4), 20D.3 (A5), 20E.14 (I/O4), 20E.3 (A5), 21B.14 (I/O4), 21B.3 (A5), 21C.14 (I/O4), 21C.3 (A5), 21D.14 (I/O4), 21D.3 (A5), 21E.14 (I/O4), 21E.3 (A5), 23E.13 (5D)
- new net SD0: 17A.13 (QH)
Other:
- moved on the sheet: 13D, 14A, 14C, 14E, 14F, 15A, 15H, 16A, 16E, 16H, 17A, 17C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
